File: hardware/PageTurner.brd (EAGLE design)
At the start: 100 x 80 mm, 11 parts

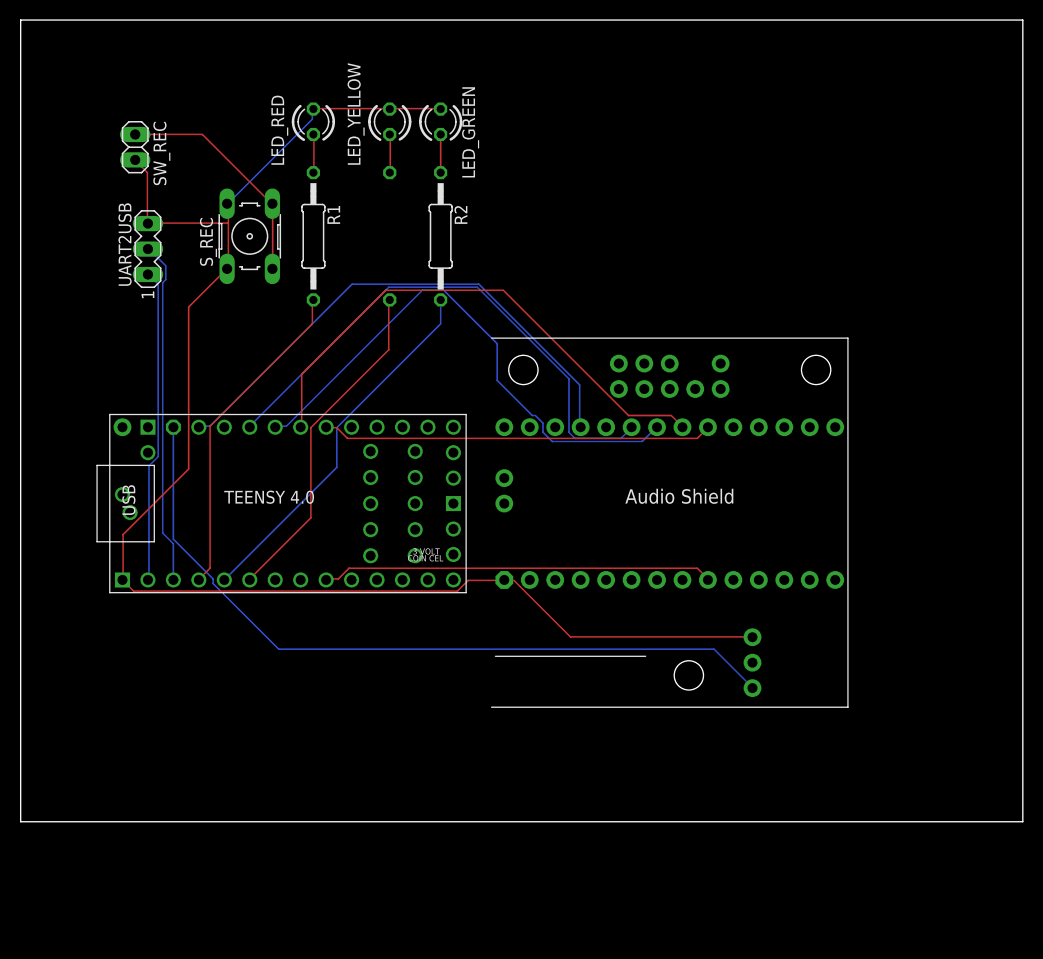
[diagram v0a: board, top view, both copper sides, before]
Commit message: Mic input routed to headphones works
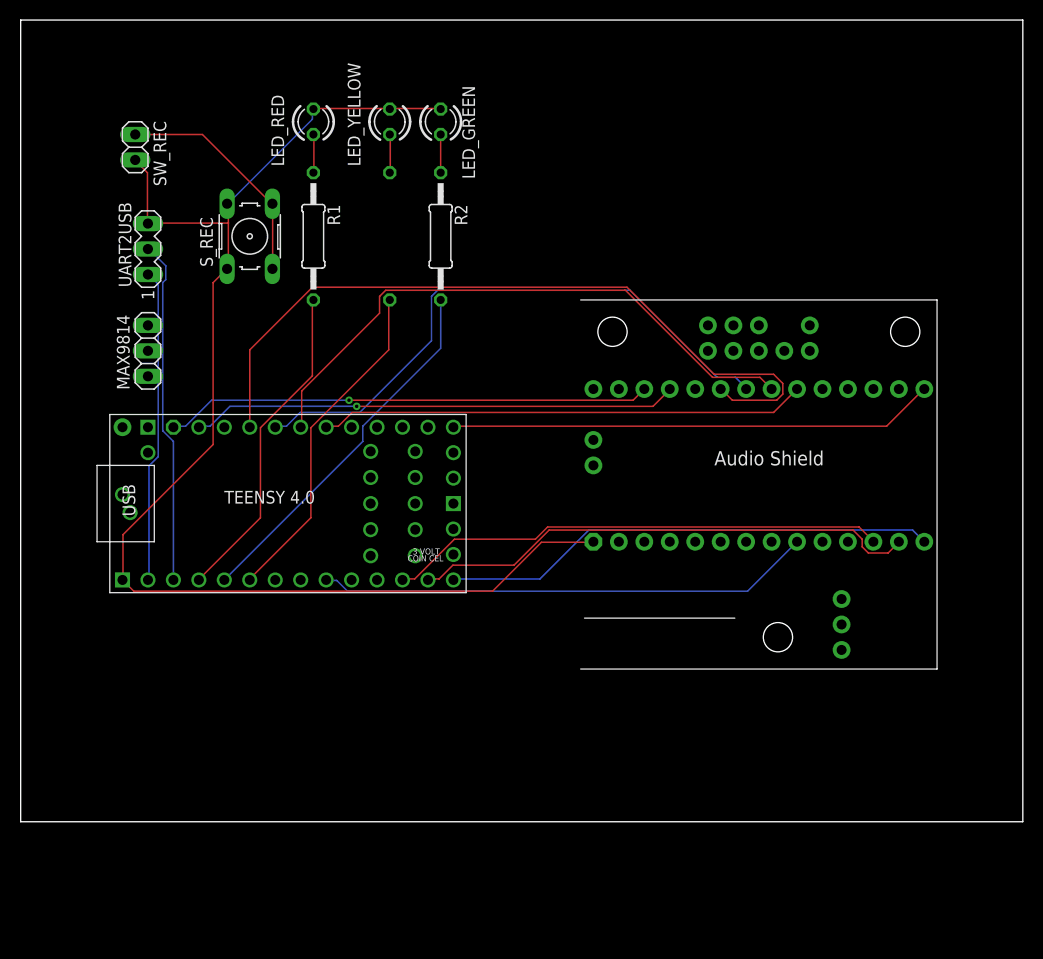
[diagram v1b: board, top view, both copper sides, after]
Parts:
- added MAX9814: (no value), pinhead:1X03
- moved U$2 9.67 mm to (73.7, 33.0)
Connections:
- removed net N$18: U$1.3V3-1, U$2.VOL_3.3V
- new net 3.3V: MAX9814.2, U$1.3V3-1, U$2.3V
- new net GND: MAX9814.1, U$2.INGND1
- new net N$17: U$1.10-CS/MQSR, U$2.10
- new net N$19: U$1.11-MOSI/CTX1, U$2.11
- new net N$20: U$1.12-MIO/MQSL, U$2.12
- new net N$21: U$1.13-SCK/CRX1/LED, U$2.13
- new net OUT: MAX9814.3, U$2.INL
- net N$7: now also U$2.G; no longer U$2.VOL_GND
- net N$9: now also U$1.5-IN2
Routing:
- net N$18: track 75.4 -> 0.00 mm
- net N$19: track 0.00 -> 51.0 mm
- net N$17: track 0.00 -> 49.9 mm
- net N$20: track 0.00 -> 49.5 mm
- net 3.3V: track 0.00 -> 48.6 mm, vias 0 -> 1
- net N$21: track 0.00 -> 48.6 mm
- net N$12: track 53.8 -> 75.4 mm
- net N$7: track 149.0 -> 132.4 mm
- net N$15: track 39.2 -> 49.5 mm
- net N$16: track 39.1 -> 48.6 mm
- net N$14: track 52.5 -> 59.8 mm
- net N$13: track 53.3 -> 59.4 mm
- net N$11: track 52.4 -> 48.6 mm, vias 0 -> 1

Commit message: preparations for futrue improvements
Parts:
- removed LED_GREEN, LED_RED, LED_YELLOW: (no value), led:LED3MM
- removed R1, R2, R3: 470, rcl:0207/12
- removed SW_REC: (no value), pinhead:1X02
- removed S_REC: (no value), switch-omron:B3F-10XX
- removed UART2USB: (no value), con-lstb:MA03-1
- added BLUEFRUIT: (no value), pinhead:1X04
- added LOGOUTPUT: (no value), con-lstb:MA03-1
- added SV1: (no value), con-lsta:FE08
- moved U$2 54.7 mm to (19.1, 29.2)
- moved MAX9814 35.6 mm to (48.3, 45.7)
- moved U$1 7.62 mm to (19.1, 31.8)
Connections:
- removed net N$13: U$1.20-A6/TX5/LRCLK1, U$2.20
- removed net N$14: U$1.19-A5/SCL0, U$2.19
- removed net N$15: U$1.7-RX2/OUT1A, U$2.7
- removed net N$16: U$1.18-A4/SDA0, U$2.18
- removed net N$17: U$1.10-CS/MQSR, U$2.10
- removed net N$19: U$1.11-MOSI/CTX1, U$2.11
- removed net N$20: U$1.12-MIO/MQSL, U$2.12
- removed net N$21: U$1.13-SCK/CRX1/LED, U$2.13
- removed net N$4: LED_YELLOW.A, R3.1
- removed net N$7: LED_GREEN.K, LED_RED.K, LED_YELLOW.K, SW_REC.2, S_REC.1, S_REC.2, U$1.GND1, U$2.G, U$2.GND, UART2USB.3
- new net 3V: MAX9814.2, U$2.3V
- new net BLE_RX: BLUEFRUIT.3, U$1.17-A3/TX4/SDA1
- new net BLE_TX: BLUEFRUIT.4, U$1.16-A2/RX4/SCL1
- net 3.3V: now also BLUEFRUIT.2; no longer MAX9814.2, U$2.3V
- net GND: now also BLUEFRUIT.1, LOGOUTPUT.3, SV1.1, U$1.GND1; no longer U$2.INGND1
- net N$1: now also SV1.2; no longer R1.2
- net N$10: now also LOGOUTPUT.2; no longer UART2USB.2
- net N$11: now also SV1.5, U$1.5-IN2; no longer U$1.23-A9/CRX1/CCLK1, U$2.23
- net N$12: now also SV1.6, U$1.15-A1/RX3/S-PDIF_IN; no longer U$1.21-A7/RX5/BCLK1, U$2.21
- net N$2: now also SV1.7; no longer R2.2, U$1.3-LRCLK2
- net N$3: now also SV1.8, U$1.9-OUT1C; no longer R3.2, U$1.4-BCLK2
- net N$5: now also U$1.14-A0/TX3/S-PFI_OUT; no longer LED_GREEN.A, R2.1
- net N$6: now also SV1.3, U$1.3-LRCLK2; no longer LED_RED.A, R1.1
- net N$8: now also LOGOUTPUT.1; no longer UART2USB.1
- net N$9: now also SV1.4, U$1.4-BCLK2; no longer SW_REC.1, S_REC.3, S_REC.4, U$1.5-IN2
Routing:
- net N$7: track 132.4 -> 0.00 mm
- net GND: track 0.00 -> 77.6 mm
- net N$14: track 59.8 -> 0.00 mm
- net N$13: track 59.4 -> 0.00 mm
- net N$19: track 51.0 -> 0.00 mm
- net N$17: track 49.9 -> 0.00 mm
- net N$20: track 49.5 -> 0.00 mm
- net N$15: track 49.5 -> 0.00 mm
- net N$16: track 48.6 -> 0.00 mm
- net N$21: track 48.6 -> 0.00 mm
- net N$12: track 75.4 -> 33.2 mm
- net N$2: track 36.9 -> 0.00 mm
- net N$6: track 3.91 -> 38.0 mm
- net BLE_RX: track 0.00 -> 30.8 mm
- net BLE_TX: track 0.00 -> 30.0 mm
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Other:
- board size 100 x 80 mm -> 63.2 x 64.8 mm

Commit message: separated some AI classes for better recall
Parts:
- added C1: 10uF, rcl:E2-4
- added C2, C3: 100nF, rcl:C025-040X050
- added L1: 100uF, rcl:0207/5V
- added R1: 820, rcl:0207/7
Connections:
- new net N$4: MAX9814.3, R1.2
- new net N$7: C1.+, C2.1, L1.2, MAX9814.2
- net 3V: now also L1.1; no longer MAX9814.2
- net GND: now also C1.-, C2.2, C3.2
- net OUT: now also C3.1, R1.1; no longer MAX9814.3
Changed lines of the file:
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@@
 <attribute name="VALUE" x="45.339" y="27.94" size="1.27" layer="27" ratio="10" rot="R270"/>
+</element>
+<element name="R1" library="rcl" library_urn="urn:adsk.eagle:library:334" package="0207/7" package3d_urn="urn:adsk.eagle:package:23493/2" value="820" x="19.05" y="52.07" smashed="yes">
+<attribute name="NAME" x="16.51" y="53.467" size="1.27" layer="25" ratio="10"/>
+<attribute name="POPULARITY" value="46" x="19.05" y="52.07" size="1.778" layer="27" display="off"/>
+<attribute name="SPICEPREFIX" value="R" x="19.05" y="52.07" size="1.778" layer="27" display="off"/>
+<attribute name="VALUE" x="16.764" y="51.5112" size="1.27" layer="27" ratio="10"/>
+</element>
+<element name="C1" library="rcl" library_urn="urn:adsk.eagle:library:334" package="E2-4" package3d_urn="urn:adsk.eagle:package:23347/1" value="10uF" x="30.48" y="55.88" smashed="yes">
+<attribute name="NAME" x="32.639" y="56.769" size="1.27" layer="25" ratio="10"/>
+<attribute name="POPULARITY" value="7" x="30.48" y="55.88" size="1.778" layer="27" display="off"/>
+<attribute name="SPICEPREFIX" value="C" x="30.48" y="55.88" size="1.778" layer="27" display="off"/>
+<attribute name="VALUE" x="32.639" y="53.721" size="1.27" layer="27" ratio="10"/>
+</element>
+<element name="C2" library="rcl" library_urn="urn:adsk.eagle:library:334" package="C025-040X050" package3d_urn="urn:adsk.eagle:package:23634/1" value="100nF" x="17.78" y="58.42" smashed="yes">
+<attribute name="NAME" x="15.494" y="60.579" size="1.27" layer="25" ratio="10"/>
+<attribute name="POPULARITY" value="4" x="17.78" y="58.42" size="1.778" layer="27" display="off"/>
+<attribute name="SPICEPREFIX" value="C" x="17.78" y="58.42" size="1.778" layer="27" display="off"/>
+<attribute name="VALUE" x="15.494" y="54.991" size="1.27" layer="27" ratio="10"/>
+</element>
+<element name="L1" library="rcl" library_urn="urn:adsk.eagle:library:334" package="0207/5V" package3d_urn="urn:adsk.eagle:package:23502/1" value="100uF" x="10.16" y="55.88" smashed="yes">
+<attribute name="NAME" x="9.017" y="56.769" size="1.27" layer="25" ratio="10"/>
+<attribute name="POPULARITY" value="1" x="10.16" y="55.88" size="1.778" layer="27" display="off"/>
+<attribute name="SPICEPREFIX" value="L" x="10.16" y="55.88" size="1.778" layer="27" display="off"/>
+<attribute name="VALUE" x="9.017" y="53.721" size="1.27" layer="27" ratio="10"/>
+</element>
+<element name="C3" library="rcl" library_urn="urn:adsk.eagle:library:334" package="C025-040X050" package3d_urn="urn:adsk.eagle:package:23634/1" value="100nF" x="25.4" y="59.69" smashed="yes">
+<attribute name="NAME" x="23.114" y="61.849" size="1.27" layer="25" ratio="10"/>
+<attribute name="POPULARITY" value="4" x="25.4" y="59.69" size="1.778" layer="27" display="off"/>
+<attribute name="SPICEPREFIX" value="C" x="25.4" y="59.69" size="1.778" layer="27" display="off"/>
+<attribute name="VALUE" x="23.114" y="56.261" size="1.27" layer="27" ratio="10"/>
 </element>
 </elements>
@@
 <wire x1="48.26" y1="43.2816" x2="46.4312" y2="45.1104" width="0.254" layer="1"/>
 <wire x1="48.26" y1="43.2816" x2="48.26" y2="43.18" width="0.254" layer="1"/>
+<contactref element="C1" pad="-"/>
+<contactref element="C2" pad="2"/>
+<contactref element="C3" pad="2"/>
+<wire x1="19.05" y1="58.42" x2="2.54" y2="24.13" width="0" layer="19" extent="1-1"/>
+<wire x1="31.496" y1="55.88" x2="19.05" y2="58.42" width="0" layer="19" extent="1-1"/>
+<wire x1="26.67" y1="59.69" x2="19.05" y2="58.42" width="0" layer="19" extent="1-1"/>
 </signal>
 <signal name="3.3V">
@@
 </signal>
 <signal name="OUT">
-<contactref element="MAX9814" pad="3"/>
 <contactref element="U$2" pad="INL"/>
-<wire x1="48.26" y1="48.1584" x2="48.26" y2="48.26" width="0.254" layer="1"/>
 <wire x1="13.97" y1="43.18" x2="15.6972" y2="44.9072" width="0.254" layer="1"/>
-<wire x1="15.6972" y1="44.9072" x2="48.26" y2="48.1584" width="0" layer="19" extent="1-1"/>
+<contactref element="R1" pad="1"/>
+<contactref element="C3" pad="1"/>
+<wire x1="15.24" y1="52.07" x2="13.97" y2="43.18" width="0" layer="19" extent="1-1"/>
+<wire x1="24.13" y1="59.69" x2="15.24" y2="52.07" width="0" layer="19" extent="1-1"/>
 </signal>
 <signal name="N$3">
@@
 </signal>
 <signal name="3V">
-<contactref element="MAX9814" pad="2"/>
 <contactref element="U$2" pad="3V"/>
 <wire x1="7.62" y1="39.5224" x2="7.62" y2="39.37" width="0.254" layer="16"/>
-<wire x1="7.62" y1="39.5224" x2="48.26" y2="45.72" width="0" layer="19" extent="16-16"/>
+<contactref element="L1" pad="1"/>
+<wire x1="7.62" y1="55.88" x2="7.62" y2="39.37" width="0" layer="19" extent="1-1"/>
 </signal>
 <signal name="N$6">
@@
 <contactref element="SV1" pad="7"/>
 </signal>
+<signal name="N$4">
+<contactref element="MAX9814" pad="3"/>
+<wire x1="48.26" y1="48.1584" x2="48.26" y2="48.26" width="0.254" layer="1"/>
+<contactref element="R1" pad="2"/>
+<wire x1="22.86" y1="52.07" x2="48.26" y2="48.1584" width="0" layer="19" extent="1-1"/>
+</signal>
+<signal name="N$7">
+<contactref element="MAX9814" pad="2"/>
+<contactref element="C1" pad="+"/>
+<contactref element="C2" pad="1"/>
+<contactref element="L1" pad="2"/>
+<wire x1="29.464" y1="55.88" x2="48.26" y2="45.72" width="0" layer="19" extent="1-1"/>
+<wire x1="12.7" y1="55.88" x2="29.464" y2="55.88" width="0" layer="19" extent="1-1"/>
+<wire x1="16.51" y1="58.42" x2="12.7" y2="55.88" width="0" layer="19" extent="1-1"/>
+</signal>
 </signals>

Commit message: trained new model and made python programm not crashing if teensy connection breaks
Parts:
- removed SV1: (no value), con-lsta:FE08
- added ON_OFF_PANEL, PAGE_LEDS: (no value), con-lstb:MA04-1
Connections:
- net N$10 renamed LOG_TX
- net N$8 renamed LOG_RX
- removed net N$11: SV1.5, U$1.5-IN2
- removed net N$12: SV1.6, U$1.15-A1/RX3/S-PDIF_IN
- removed net N$9: SV1.4, U$1.4-BCLK2
- new net N$8: PAGE_LEDS.2, U$1.3-LRCLK2
- net GND: now also ON_OFF_PANEL.1, PAGE_LEDS.1; no longer SV1.1
- net N$1: now also PAGE_LEDS.3; no longer SV1.2
- net N$2: now also PAGE_LEDS.4, U$1.14-A0/TX3/S-PFI_OUT; no longer SV1.7
- net N$3: now also ON_OFF_PANEL.4, U$1.15-A1/RX3/S-PDIF_IN; no longer SV1.8, U$1.9-OUT1C
- net N$5: now also ON_OFF_PANEL.3, U$1.5-IN2; no longer U$1.14-A0/TX3/S-PFI_OUT
- net N$6: now also ON_OFF_PANEL.2, U$1.22-A8/CTX1; no longer SV1.3, U$1.3-LRCLK2
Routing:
- net N$6: track 38.0 -> 0.00 mm
- net N$8: track 0.00 -> 37.8 mm
- net N$9: track 36.3 -> 0.00 mm
- net N$11: track 33.8 -> 0.00 mm
- net N$12: track 33.2 -> 0.00 mm
- net N$3: track 26.8 -> 0.00 mm
- net GND: track 77.6 -> 73.4 mm
